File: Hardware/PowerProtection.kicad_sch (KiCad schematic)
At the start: 17 parts, among them IC5 LM76202QPWPRQ1

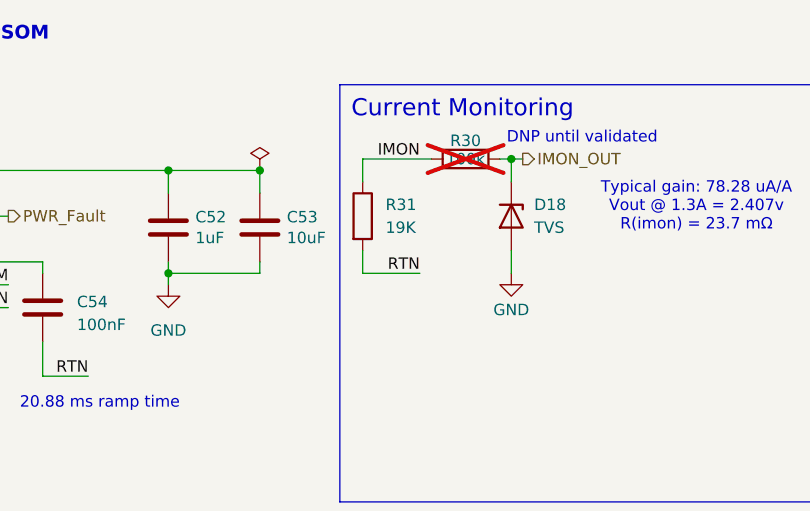
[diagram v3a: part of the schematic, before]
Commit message: updated some component part nums
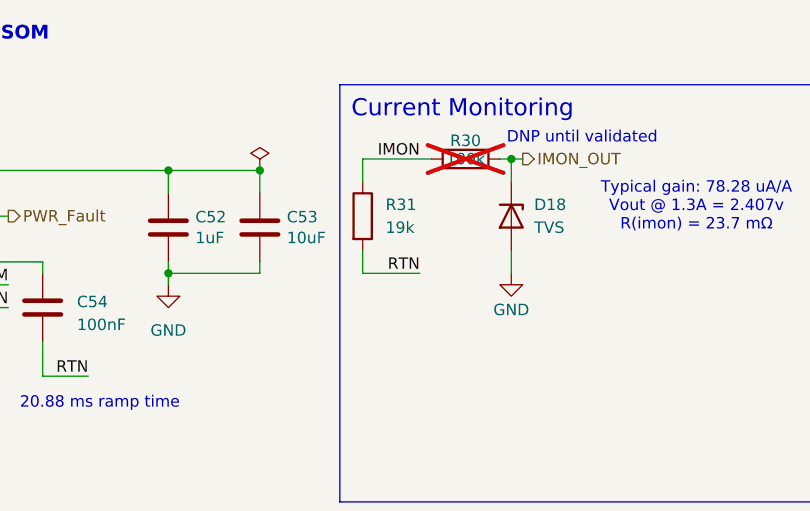
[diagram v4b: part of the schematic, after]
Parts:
- C50, C53: Mfg (none) -> GRM21BR61H106KE43K
- C51, C52: Mfg (none) -> MLASU168SB5105KTNA01
- C54: Mfg (none) -> MLASH168SB7104KTNA01
- R30: Mfg (none) -> CRCW0603100KFKEE; P/N CRCW0603100KFKEE -> CRCW0603100KFKEE
- R31: value 19K -> 19k
- R32, R33, R34: Mfg (none) -> CRCW060310K0FKEI
- R35: Mfg (none) -> CRCW0603402KFKEAC
- R36: Mfg (none) -> CRCW060345K3FKEAHP
- R37: Mfg (none) -> CRCW0603590RFKEA
- R38: Mfg (none) -> CRCW06032K10FKEA
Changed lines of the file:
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@@
+			)
+		)
+		(property "Mfg" "MLASH168SB7104KTNA01"
+			(at 106.68 46.99 0)
+			(effects
+				(font
+					(size 1.27 1.27)
+				)
+				(hide yes)
 			)
 		)
@@
 			)
 		)
+		(property "Mfg" "CRCW060345K3FKEAHP "
+			(at 21.59 102.87 0)
+			(effects
+				(font
+					(size 1.27 1.27)
+				)
+				(hide yes)
+			)
+		)
 		(pin "1"
 		)
@@
 			)
 		)
+		(property "Mfg" "CRCW06032K10FKEA "
+			(at 21.59 123.19 0)
+			(effects
+				(font
+					(size 1.27 1.27)
+				)
+				(hide yes)
+			)
+		)
 		(pin "1"
 		)
@@
 		)
 		(property "P/N" "GRM21BR61H106KE43K"
+			(at 29.21 36.83 0)
+			(effects
+				(font
+					(size 1.27 1.27)
+				)
+				(hide yes)
+			)
+		)
+		(property "Mfg" "GRM21BR61H106KE43K"
 			(at 29.21 36.83 0)
 			(effects
@@
 			)
 		)
-		(property "Value" "19K"
+		(property "Value" "19k"
 			(at 144.78 38.0999 0)
 			(effects
@@
 			)
 		)
+		(property "Mfg" "CRCW060310K0FKEI "
+			(at 36.83 68.58 0)
+			(effects
+				(font
+					(size 1.27 1.27)
+				)
+				(hide yes)
+			)
+		)
 		(pin "1"
 		)
@@
 			)
 		)
+		(property "Mfg" "CRCW0603402KFKEAC "
+			(at 129.54 92.71 0)
+			(effects
+				(font
+					(size 1.27 1.27)
+				)
+				(hide yes)
+			)
+		)
 		(pin "1"
 		)
@@
 			)
 		)
-		(property "P/N" "CRCW0603100KFKEE "
+		(property "P/N" "CRCW0603100KFKEE"
+			(at 153.67 30.48 90)
+			(effects
+				(font
+					(size 1.27 1.27)
+				)
+				(hide yes)
+			)
+		)
+		(property "Mfg" "CRCW0603100KFKEE"
 			(at 153.67 30.48 90)
 			(effects
@@
 			)
 		)
+		(property "Mfg" "CRCW060310K0FKEI "
+			(at 146.05 88.9 0)
+			(effects
+				(font
+					(size 1.27 1.27)
+				)
+				(hide yes)
+			)
+		)
 		(pin "1"
 		)
@@
 		)
 		(property "P/N" "GRM21BR61H106KE43K"
+			(at 130.81 38.1 0)
+			(effects
+				(font
+					(size 1.27 1.27)
+				)
+				(hide yes)
+			)
+		)
+		(property "Mfg" "GRM21BR61H106KE43K"
 			(at 130.81 38.1 0)
 			(effects
@@
 			)
 		)
+		(property "Mfg" "CRCW0603590RFKEA"
+			(at 21.59 113.03 0)
+			(effects
+				(font
+					(size 1.27 1.27)
+				)
+				(hide yes)
+			)
+		)
 		(pin "1"
 		)
@@
 			)
 		)
+		(property "Mfg" "CRCW060310K0FKEI "
+			(at 160.02 88.9 0)
+			(effects
+				(font
+					(size 1.27 1.27)
+				)
+				(hide yes)
+			)
+		)
 		(pin "1"
 		)
@@
 			)
 		)
+		(property "Mfg" "MLASU168SB5105KTNA01"
+			(at 120.65 38.1 0)
+			(effects
+				(font
+					(size 1.27 1.27)
+				)
+				(hide yes)
+			)
+		)
 		(pin "1"
 		)
@@
 			(at 40.64 36.83 0)
 			(effects
+				(font
+					(size 1.27 1.27)
+				)
+				(hide yes)
+			)
+		)
+		(property "Mfg" "MLASU168SB5105KTNA01"
+			(at 40.64 36.83 0)
+			(effects

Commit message: generated production stuff
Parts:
- R31: Mfg (none) -> MCT06030C1912FP500; P/N WFCP0603R0240FE66 -> MCT06030C1912FP500
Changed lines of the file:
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@@
 			)
 		)
-		(property "P/N" "WFCP0603R0240FE66"
+		(property "P/N" "MCT06030C1912FP500"
 			(at 142.24 36.83 0)
 			(effects
+				(font
+					(size 1.27 1.27)
+				)
+				(hide yes)
+			)
+		)
+		(property "Mfg" "MCT06030C1912FP500"
+			(at 142.24 36.83 0)
+			(effects
